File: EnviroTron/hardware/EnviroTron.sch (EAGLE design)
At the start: 29 parts

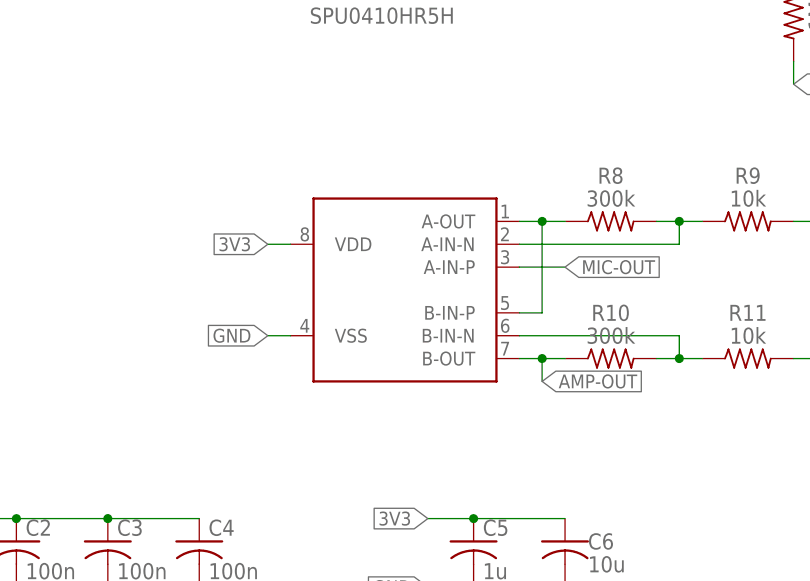
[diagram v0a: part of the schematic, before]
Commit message: Reorganized files into project based structures
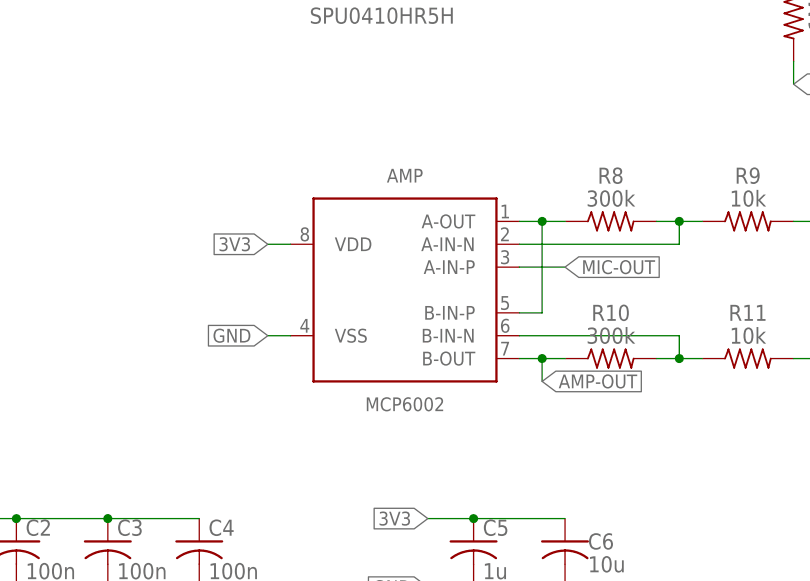
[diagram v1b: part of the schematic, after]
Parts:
- renumbered U$1 to AMP
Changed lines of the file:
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@@
 <part name="C7" library="SmslsTron-1" deviceset="C-US" device="C0603" value="100n"/>
 <part name="SOUND" library="EnviroTron" deviceset="SPU0410HR5H" device=""/>
-<part name="U$1" library="EnviroTron" deviceset="MCP6002" device=""/>
+<part name="AMP" library="EnviroTron" deviceset="MCP6002" device=""/>
 <part name="C8" library="SmslsTron-1" deviceset="C-US" device="C0603" value="1u"/>
 <part name="C9" library="SmslsTron-1" deviceset="C-US" device="C0603" value="1u"/>
@@
 <instance part="C7" gate="G$1" x="78.74" y="-5.08"/>
 <instance part="SOUND" gate="G$1" x="139.7" y="63.5"/>
-<instance part="U$1" gate="G$1" x="142.24" y="22.86"/>
+<instance part="AMP" gate="G$1" x="142.24" y="22.86"/>
 <instance part="C8" gate="G$1" x="190.5" y="30.48" rot="R90"/>
 <instance part="C9" gate="G$1" x="190.5" y="15.24" rot="R90"/>
@@
 <wire x1="129.54" y1="27.94" x2="127" y2="27.94" width="0.1524" layer="91"/>
 <label x="127" y="27.94" size="1.524" layer="95" rot="R180" xref="yes"/>
-<pinref part="U$1" gate="G$1" pin="VDD"/>
+<pinref part="AMP" gate="G$1" pin="VDD"/>
 </segment>
 <segment>
@@
 <wire x1="129.54" y1="17.78" x2="127" y2="17.78" width="0.1524" layer="91"/>
 <label x="127" y="17.78" size="1.524" layer="95" rot="R180" xref="yes"/>
-<pinref part="U$1" gate="G$1" pin="VSS"/>
+<pinref part="AMP" gate="G$1" pin="VSS"/>
 </segment>
 <segment>
@@
 </segment>
 <segment>
-<pinref part="U$1" gate="G$1" pin="A-IN-P"/>
+<pinref part="AMP" gate="G$1" pin="A-IN-P"/>
 <wire x1="154.94" y1="25.4" x2="160.02" y2="25.4" width="0.1524" layer="91"/>
 <label x="160.02" y="25.4" size="1.524" layer="95" xref="yes"/>
@@
 <net name="N$2" class="0">
 <segment>
-<pinref part="U$1" gate="G$1" pin="A-OUT"/>
+<pinref part="AMP" gate="G$1" pin="A-OUT"/>
 <pinref part="R8" gate="G$1" pin="1"/>
 <wire x1="154.94" y1="30.48" x2="157.48" y2="30.48" width="0.1524" layer="91"/>
@@
 <wire x1="157.48" y1="30.48" x2="157.48" y2="20.32" width="0.1524" layer="91"/>
 <junction x="157.48" y="30.48"/>
-<pinref part="U$1" gate="G$1" pin="B-IN-P"/>
+<pinref part="AMP" gate="G$1" pin="B-IN-P"/>
 <wire x1="157.48" y1="20.32" x2="154.94" y2="20.32" width="0.1524" layer="91"/>
 </segment>
@@
 <pinref part="R9" gate="G$1" pin="1"/>
 <wire x1="170.18" y1="30.48" x2="172.72" y2="30.48" width="0.1524" layer="91"/>
-<pinref part="U$1" gate="G$1" pin="A-IN-N"/>
+<pinref part="AMP" gate="G$1" pin="A-IN-N"/>
 <wire x1="172.72" y1="30.48" x2="175.26" y2="30.48" width="0.1524" layer="91"/>
 <wire x1="154.94" y1="27.94" x2="172.72" y2="27.94" width="0.1524" layer="91"/>
@@
 <net name="AMP-OUT" class="0">
 <segment>
-<pinref part="U$1" gate="G$1" pin="B-OUT"/>
+<pinref part="AMP" gate="G$1" pin="B-OUT"/>
 <pinref part="R10" gate="G$1" pin="1"/>
 <wire x1="154.94" y1="15.24" x2="157.48" y2="15.24" width="0.1524" layer="91"/>
@@
 <pinref part="R11" gate="G$1" pin="1"/>
 <wire x1="170.18" y1="15.24" x2="172.72" y2="15.24" width="0.1524" layer="91"/>
-<pinref part="U$1" gate="G$1" pin="B-IN-N"/>
+<pinref part="AMP" gate="G$1" pin="B-IN-N"/>
 <wire x1="172.72" y1="15.24" x2="175.26" y2="15.24" width="0.1524" layer="91"/>
 <wire x1="154.94" y1="17.78" x2="172.72" y2="17.78" width="0.1524" layer="91"/>

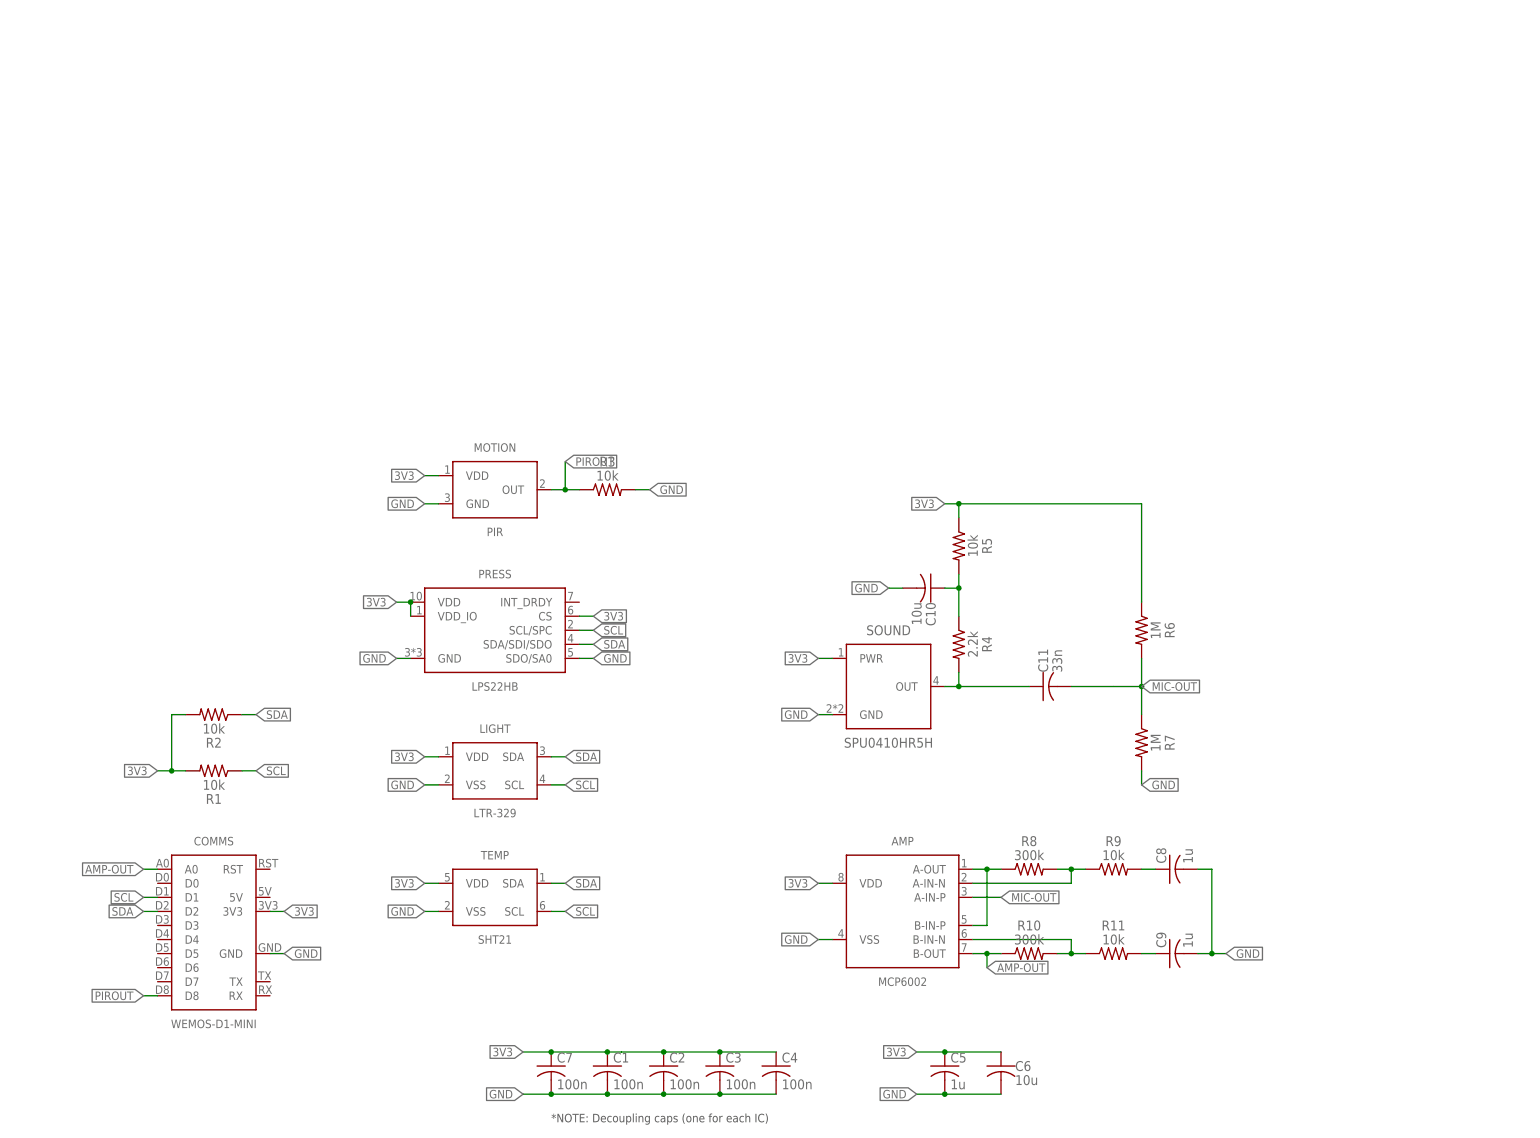
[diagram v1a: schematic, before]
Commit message: Added MUX to allow for hardware defined device IDs. Moved PIR input to pin that doesn't affect bootloader operation.
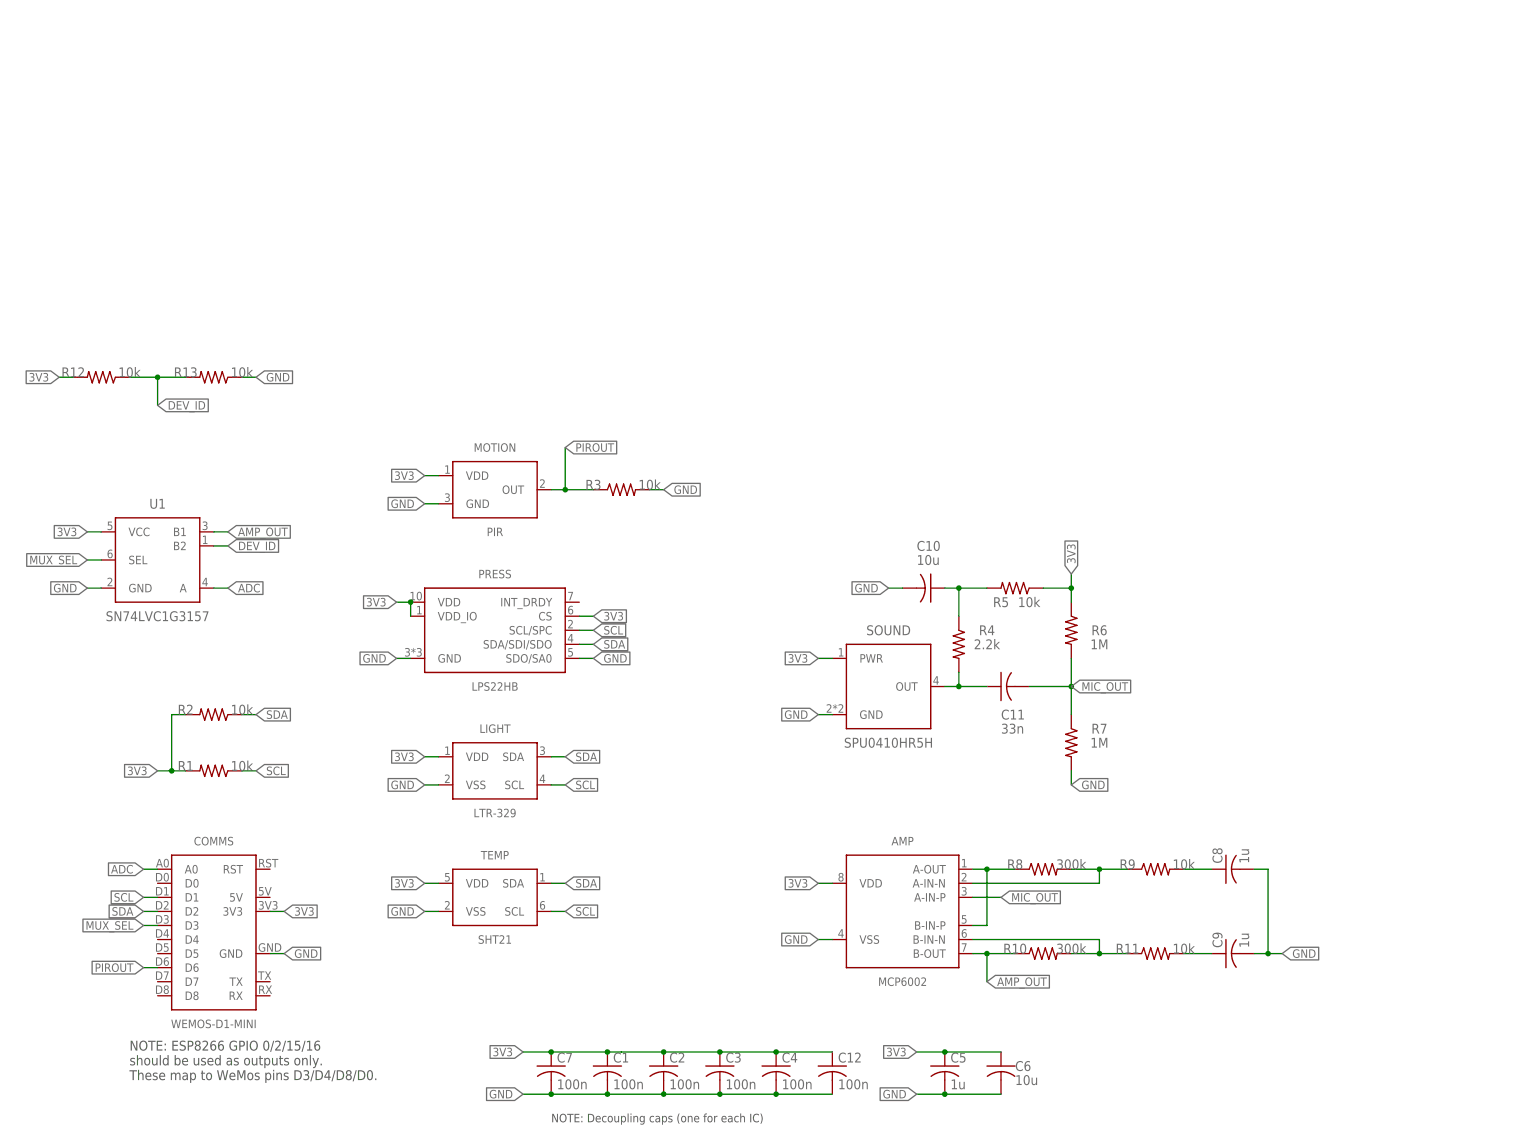
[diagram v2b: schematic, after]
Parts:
- added C12: 100n, SmslsTron-1:C-USC0603
- added R12, R13: 10k, SmslsTron-1:R-US_R0603
- added U1: SN74LVC1G3157, EnviroTron:SN74LVC1G3157
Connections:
- net MIC-OUT renamed MIC_OUT
- removed net AMP-OUT: AMP.B-OUT, COMMS.A0, R10.1
- new net ADC: COMMS.A0, U1.A
- new net AMP_OUT: AMP.B-OUT, R10.1, U1.B1
- new net DEV_ID: R12.1, R13.2, U1.B2
- new net MUX_SEL: COMMS.D3, U1.SEL
- net 3V3: now also C12.1, R12.2, U1.VCC
- net GND: now also C12.2, R13.1, U1.GND
- net PIROUT: now also COMMS.D6; no longer COMMS.D8
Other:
- note added: "NOTE: Decoupling caps (one for each IC)"
- note added: "NOTE: ESP8266 GPIO 0/2/15/16 should be used as outputs only. These map to WeMos pins D3/D4/D8/D0."
- note removed: "*NOTE: Decoupling caps (one for each IC)"
- moved on the sheet: C11, C8, C9, R10, R11, R3, R5, R6, R7, R8, R9

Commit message: Consolidated all parts to EnviroTron library. Cleaned up schematic and layout.
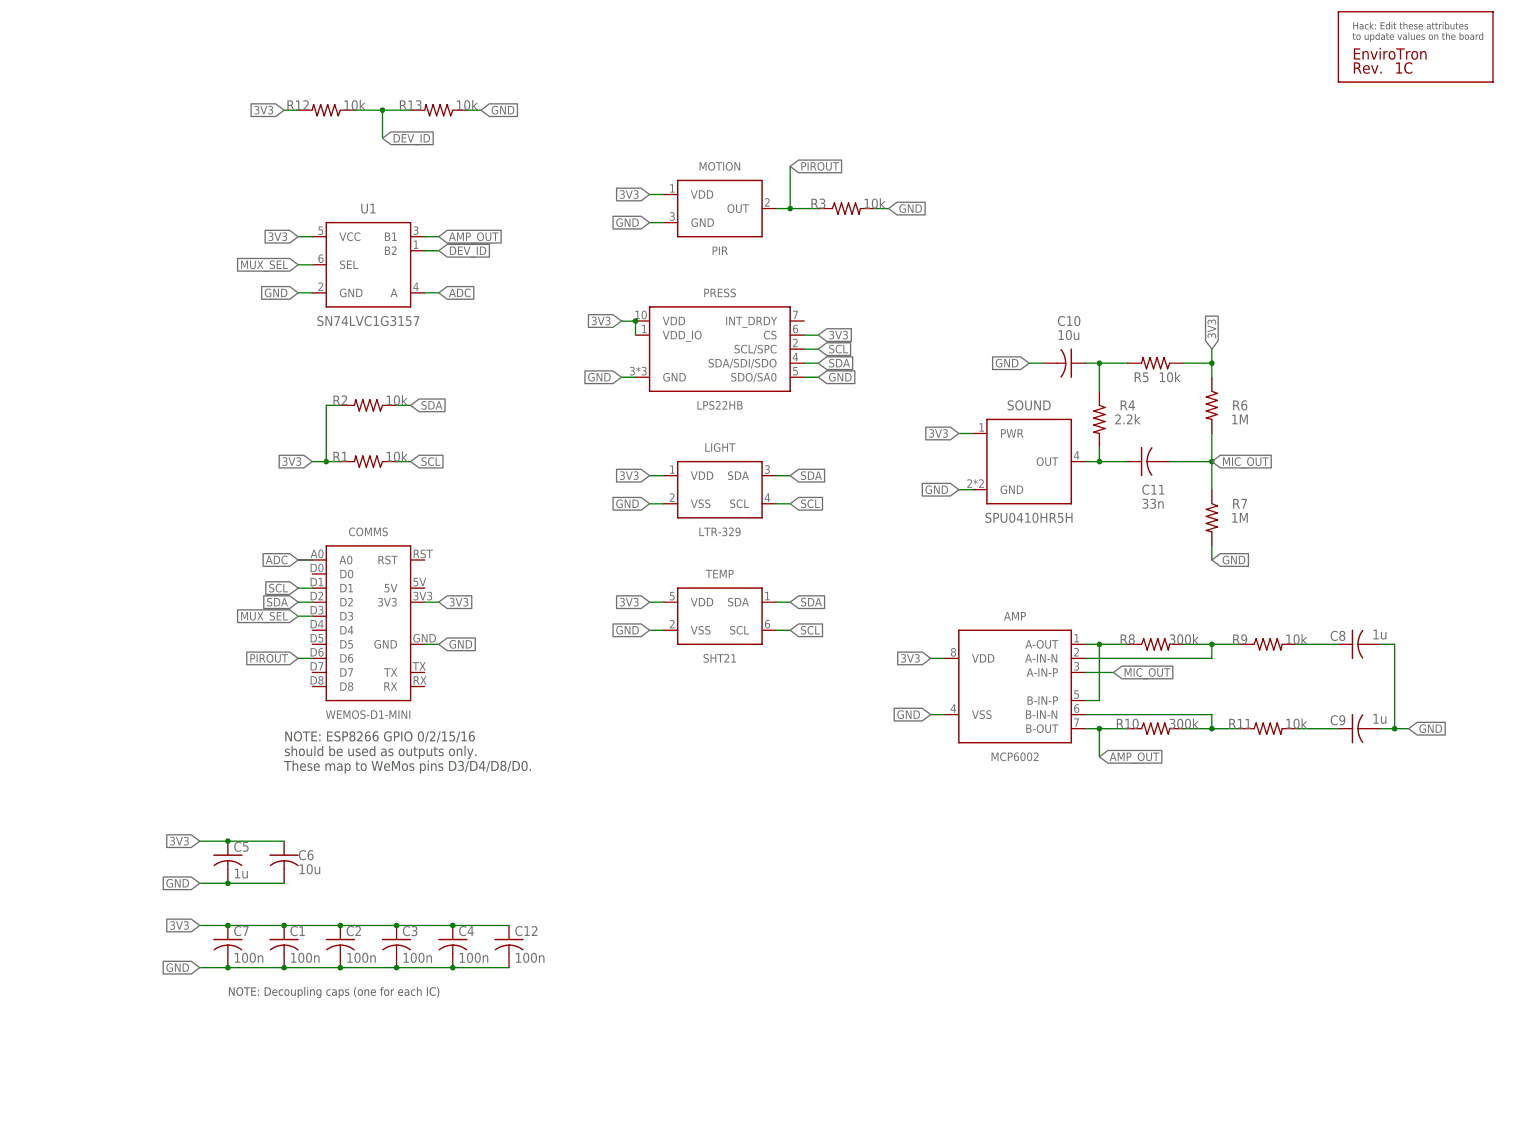
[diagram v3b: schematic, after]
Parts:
- added U$1: SILK_QC, EnviroTron:SILK_QC
- C1, C12, C2, C3, C4, C5, C7, C8, C9: device SmslsTron-1:C-USC0603 -> EnviroTron:C-USC0603
- C10, C11: device rcl:C-USC0805 -> EnviroTron:C-USC0603
- R1, R10, R11, R12, R13, R2, R3, R4, R5, R6, R7, R8, R9: device SmslsTron-1:R-US_R0603 -> EnviroTron:R-US_R0603
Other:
- moved on the sheet: AMP, C1, C12, C2, C3, C4, C5, C6, C7, C8, C9, COMMS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

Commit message: Redesigned board so that all components are on one side. Fixed some issues discovered through testing.
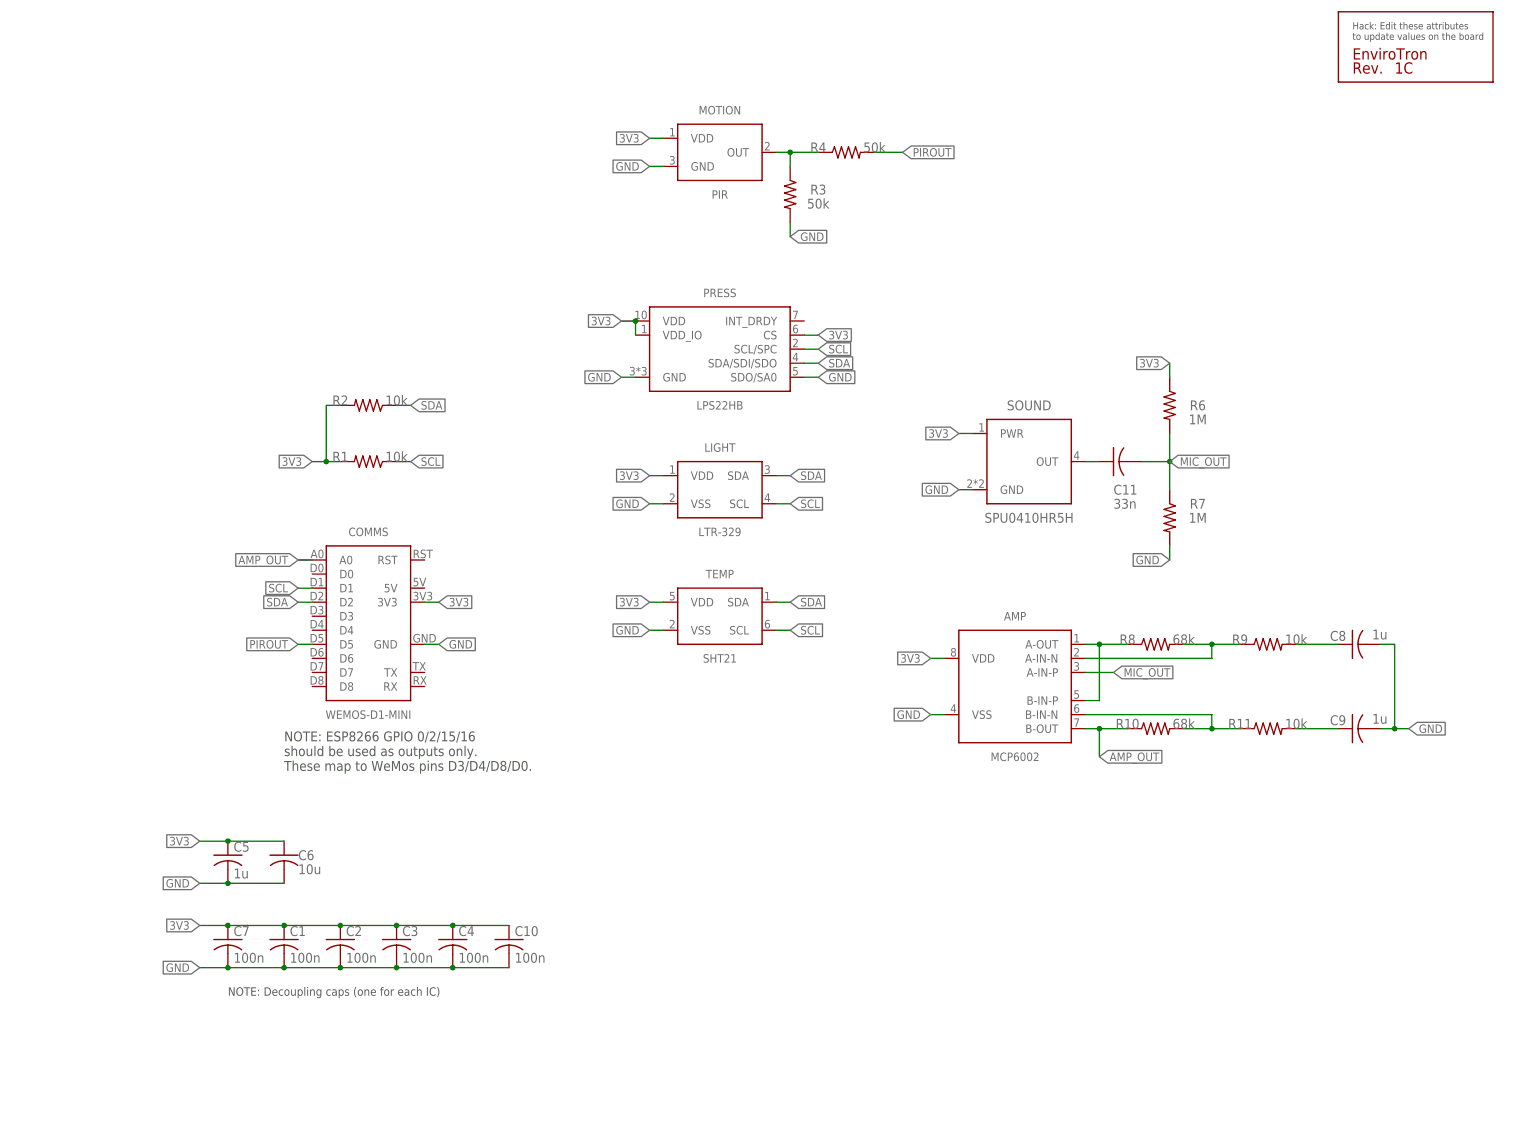
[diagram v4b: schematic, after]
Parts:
- removed C12: 100n, EnviroTron:C-USC0603
- removed R12, R13, R5: 10k, EnviroTron:R-US_R0603
- removed U1: SN74LVC1G3157, EnviroTron:SN74LVC1G3157
- C10: value 10u -> 100n
- R10, R8: value 300k -> 68k
- R3: value 10k -> 50k
- R4: value 2.2k -> 50k
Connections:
- removed net ADC: COMMS.A0, U1.A
- removed net DEV_ID: R12.1, R13.2, U1.B2
- removed net MUX_SEL: COMMS.D3, U1.SEL
- removed net N$5: C10.1, R4.1, R5.2
- new net N$3: MOTION.OUT, R3.1, R4.1
- net 3V3: now also C10.1; no longer C12.1, R12.2, R5.1, U1.VCC
- net AMP_OUT: now also COMMS.A0; no longer U1.B1
- net GND: no longer C12.2, R13.1, U1.GND
- net N$8: no longer R4.2
- net PIROUT: now also COMMS.D5, R4.2; no longer COMMS.D6, MOTION.OUT, R3.1
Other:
- moved on the sheet: C10, C11, MOTION, R3, R4, R6, R7
